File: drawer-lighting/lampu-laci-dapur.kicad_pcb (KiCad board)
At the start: 2 copper layers, 100 x 9.4 mm, 7 parts, among them P1 InPort, P3 InPad, P4 OutPad

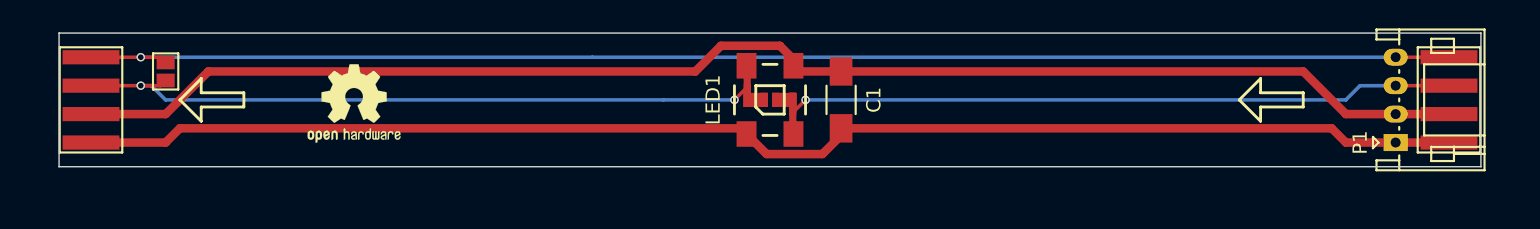
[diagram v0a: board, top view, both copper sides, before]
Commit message: Update connector pads
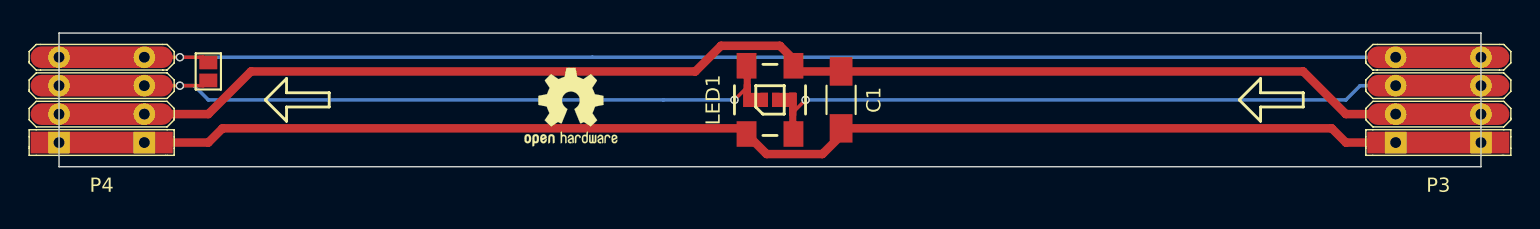
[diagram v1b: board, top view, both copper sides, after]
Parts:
- removed P1: InPort, Connectors_JST:JST_PH_S4B-PH-K_04x2.00mm_Angled
- C1: value C -> 100nF
- P3, P4: footprint Pad:FourPad_2.0mm -> Pad:FourPad_2.0mm_FrontPTH_Side
- moved REF*** 15.3 mm to (111.0, 75.5)
- moved JP1 3.00 mm to (85.5, 73.0)
- moved P3 0.75 mm to (172.0, 75.0), turned to 0 degrees
- moved P4 0.75 mm to (78.0, 75.0), turned to 0 degrees
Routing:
- net GND: track 99.7 -> 91.2 mm
- net +5V: track 100.7 -> 92.2 mm
- net /Next: track 98.4 -> 90.2 mm
- net /In: track 48.9 -> 44.7 mm
- net /Out: track 52.9 -> 48.9 mm
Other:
- board text added: "FAJRAN 2016"
- board text added: "REV 01"
- board text removed: "fajran 2016"
- board text removed: "rev01"

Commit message: Make +5V and GND traces wider
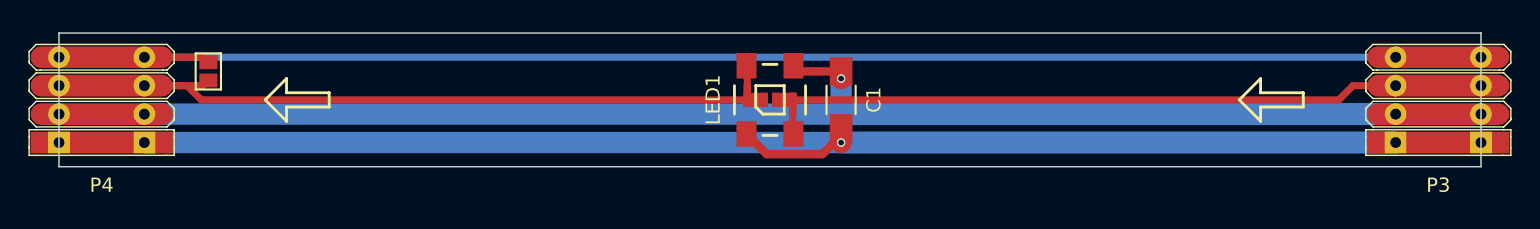
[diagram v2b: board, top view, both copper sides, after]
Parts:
- removed REF***: OSHW-Logo2_7.3x6mm_SilkScreen, Symbols:OSHW-Logo2_7.3x6mm_SilkScreen
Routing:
- net GND: track 91.2 -> 99.9 mm, vias 0 -> 1
- net /Out: track 48.9 -> 54.7 mm, vias 2 -> 0
- net +5V: track 92.2 -> 96.5 mm, vias 0 -> 1
- net /In: track 44.7 -> 48.0 mm, vias 1 -> 0
- net /Next: track 90.2 -> 92.7 mm, vias 1 -> 0
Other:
- net class +5V: trace_width 0.6 -> 1.55
- net class Default: trace_width 0.25 -> 0.5
- net class GND: trace_width 0.6 -> 1.55

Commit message: Add more traces
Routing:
- net +5V: track 96.5 -> 118.5 mm, vias 1 -> 7
- net GND: track 99.9 -> 121.9 mm, vias 1 -> 7
- net /Next: track 92.7 -> 104.7 mm
- net /Out: track 54.7 -> 60.7 mm
- net /In: track 48.0 -> 54.0 mm
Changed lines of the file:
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@@
     (thickness 1.6)
     (drawings 23)
-    (tracks 38)
+    (tracks 74)
     (zones 0)
     (modules 5)
@@
   (gr_line (start 175 70.3) (end 75 70.3) (angle 90) (layer Edge.Cuts) (width 0.1))
   (gr_line (start 75 79.7) (end 175 79.7) (angle 90) (layer Edge.Cuts) (width 0.1))
+  (segment (start 75 76) (end 77 76) (width 1.55) (layer B.Cu) (net 1))
+  (segment (start 77 76) (end 78 76) (width 1.55) (layer F.Cu) (net 1))
+  (via (at 77 76) (size 0.6) (drill 0.4) (layers F.Cu B.Cu) (net 1))
+  (via (at 78 76) (size 0.6) (drill 0.4) (layers F.Cu B.Cu) (net 1))
+  (segment (start 79 76) (end 78 76) (width 1.55) (layer F.Cu) (net 1))
+  (via (at 79 76) (size 0.6) (drill 0.4) (layers F.Cu B.Cu) (net 1))
+  (segment (start 78 76) (end 79 76) (width 1.55) (layer B.Cu) (net 1))
+  (segment (start 169 76) (end 171 76) (width 1.55) (layer B.Cu) (net 1))
+  (segment (start 171 76) (end 172 76) (width 1.55) (layer F.Cu) (net 1))
+  (via (at 171 76) (size 0.6) (drill 0.4) (layers F.Cu B.Cu) (net 1))
+  (via (at 172 76) (size 0.6) (drill 0.4) (layers F.Cu B.Cu) (net 1))
+  (segment (start 173 76) (end 172 76) (width 1.55) (layer F.Cu) (net 1))
+  (via (at 173 76) (size 0.6) (drill 0.4) (layers F.Cu B.Cu) (net 1))
+  (segment (start 172 76) (end 173 76) (width 1.55) (layer B.Cu) (net 1))
+  (segment (start 81 76) (end 75 76) (width 1.55) (layer B.Cu) (net 1))
+  (segment (start 169 76) (end 175 76) (width 1.55) (layer B.Cu) (net 1))
   (segment (start 130 76) (end 130 73.5) (width 1.5) (layer B.Cu) (net 1))
   (segment (start 130 73.5) (end 130 73) (width 1.5) (layer F.Cu) (net 1))
@@
   (segment (start 126.65 72.15) (end 126.65 72.6) (width 0.6) (layer F.Cu) (net 1))
   (segment (start 127.05 73) (end 126.65 72.6) (width 0.6) (layer F.Cu) (net 1))
+  (segment (start 75 78) (end 77 78) (width 1.55) (layer B.Cu) (net 2))
+  (segment (start 77 78) (end 78 78) (width 1.55) (layer F.Cu) (net 2))
+  (via (at 77 78) (size 0.6) (drill 0.4) (layers F.Cu B.Cu) (net 2))
+  (via (at 78 78) (size 0.6) (drill 0.4) (layers F.Cu B.Cu) (net 2))
+  (segment (start 79 78) (end 78 78) (width 1.55) (layer F.Cu) (net 2))
+  (via (at 79 78) (size 0.6) (drill 0.4) (layers F.Cu B.Cu) (net 2))
+  (segment (start 78 78) (end 79 78) (width 1.55) (layer B.Cu) (net 2))
+  (segment (start 169 78) (end 171 78) (width 1.55) (layer B.Cu) (net 2))
+  (segment (start 171 78) (end 172 78) (width 1.55) (layer F.Cu) (net 2))
+  (via (at 171 78) (size 0.6) (drill 0.4) (layers F.Cu B.Cu) (net 2))
+  (via (at 172 78) (size 0.6) (drill 0.4) (layers F.Cu B.Cu) (net 2))
+  (segment (start 173 78) (end 172 78) (width 1.55) (layer F.Cu) (net 2))
+  (via (at 173 78) (size 0.6) (drill 0.4) (layers F.Cu B.Cu) (net 2))
+  (segment (start 172 78) (end 173 78) (width 1.55) (layer B.Cu) (net 2))
+  (segment (start 81 78) (end 75 78) (width 1.55) (layer B.Cu) (net 2))
+  (segment (start 169 78) (end 175 78) (width 1.55) (layer B.Cu) (net 2))
   (segment (start 130 77) (end 130 78) (width 1.5) (layer F.Cu) (net 2))
   (via (at 130 78) (size 0.6) (drill 0.4) (layers F.Cu B.Cu) (net 2))
@@
   (segment (start 122.95 77) (end 123.35 77.4) (width 0.6) (layer F.Cu) (net 2))
   (segment (start 122.95 77) (end 123.35 77.4) (width 0.6) (layer F.Cu) (net 2))
+  (segment (start 81 74) (end 75 74) (width 0.5) (layer B.Cu) (net 3) (status C00000))
   (segment (start 78 74) (end 84 74) (width 0.5) (layer F.Cu) (net 3))
   (segment (start 84 74) (end 85 75) (width 0.5) (layer F.Cu) (net 3))
@@
   (segment (start 123.35 72.6) (end 123.35 74.15) (width 0.25) (layer F.Cu) (net 3))
   (segment (start 123.35 72.6) (end 123.35 74.65) (width 0.25) (layer F.Cu) (net 3))
+  (segment (start 169 72) (end 175 72) (width 0.5) (layer B.Cu) (net 4))
+  (segment (start 81 72) (end 75 72) (width 0.5) (layer B.Cu) (net 4))
   (segment (start 169 72) (end 81 72) (width 0.5) (layer B.Cu) (net 4))
   (segment (start 83.5 72) (end 81 72) (width 0.5) (layer F.Cu) (net 4))
   (segment (start 83.5 72) (end 85.135 72) (width 0.5) (layer F.Cu) (net 4))
   (segment (start 85.135 72) (end 85.5 72.365) (width 0.25) (layer F.Cu) (net 4))
+  (segment (start 169 74) (end 175 74) (width 0.5) (layer B.Cu) (net 5) (status C00000))
   (segment (start 126 75) (end 165 75) (width 0.5) (layer F.Cu) (net 5))
   (segment (start 165 75) (end 166 74) (width 0.5) (layer F.Cu) (net 5))
